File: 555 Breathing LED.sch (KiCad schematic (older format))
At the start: 7 parts, among them Q1 Q_NPN_BCE, U1 LMC555xN

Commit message: update
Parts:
- added BT1: Battery_Cell, Battery:BatteryHolder_Keystone_107_1x23mm, symbol Device:Battery_Cell
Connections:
- net labels added: VCC
- net labels removed: +5V
- wire segments 26 -> 28
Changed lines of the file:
@@
 Wire Wire Line
 	4300 3100 4300 2400
-Wire Wire Line
-	4300 2200 4300 2400
-Connection ~ 4300 2400
 $Comp
 L Timer:LMC555xN U1
@@
 	1    0    0    -1
 $EndComp
-$Comp
-L power:+5V #PWR0103
-U 1 1 613DEE59
-P 4300 2200
-F 0 "#PWR0103" H 4300 2050 50  0001 C CNN
-F 1 "+5V" H 4315 2373 50  0000 C CNN
-F 2 "" H 4300 2200 50  0001 C CNN
-F 3 "" H 4300 2200 50  0001 C CNN
-	1    4300 2200
-	1    0    0    -1
-$EndComp
-$Comp
-L power:+5V #PWR0104
-U 1 1 613E1C2C
-P 6750 2200
-F 0 "#PWR0104" H 6750 2050 50  0001 C CNN
-F 1 "+5V" H 6765 2373 50  0000 C CNN
-F 2 "" H 6750 2200 50  0001 C CNN
-F 3 "" H 6750 2200 50  0001 C CNN
-	1    6750 2200
-	1    0    0    -1
-$EndComp
-Wire Wire Line
-	6750 2200 6750 2500
 $Comp
 L Device:R_US R2
@@
 	6300 2700 6350 2700
 Connection ~ 6350 2700
+$Comp
+L power:GND #PWR0103
+U 1 1 613D1761
+P 3550 3800
+F 0 "#PWR0103" H 3550 3550 50  0001 C CNN
+F 1 "GND" H 3555 3627 50  0000 C CNN
+F 2 "" H 3550 3800 50  0001 C CNN
+F 3 "" H 3550 3800 50  0001 C CNN
+	1    3550 3800
+	1    0    0    -1
+$EndComp
+$Comp
+L power:VCC #PWR0104
+U 1 1 613D37AA
+P 4300 2300
+F 0 "#PWR0104" H 4300 2150 50  0001 C CNN
+F 1 "VCC" H 4315 2473 50  0000 C CNN
+F 2 "" H 4300 2300 50  0001 C CNN
+F 3 "" H 4300 2300 50  0001 C CNN
+	1    4300 2300
+	1    0    0    -1
+$EndComp
+Wire Wire Line
+	4300 2300 4300 2400
+Connection ~ 4300 2400
+$Comp
+L power:VCC #PWR0106
+U 1 1 613D7D24
+P 6750 2250
+F 0 "#PWR0106" H 6750 2100 50  0001 C CNN
+F 1 "VCC" H 6765 2423 50  0000 C CNN
+F 2 "" H 6750 2250 50  0001 C CNN
+F 3 "" H 6750 2250 50  0001 C CNN
+	1    6750 2250
+	1    0    0    -1
+$EndComp
+Wire Wire Line
+	6750 2250 6750 2500
+$Comp
+L power:VCC #PWR0107
+U 1 1 613D98F6
+P 3550 2300
+F 0 "#PWR0107" H 3550 2150 50  0001 C CNN
+F 1 "VCC" H 3565 2473 50  0000 C CNN
+F 2 "" H 3550 2300 50  0001 C CNN
+F 3 "" H 3550 2300 50  0001 C CNN
+	1    3550 2300
+	1    0    0    -1
+$EndComp
+$Comp
+L Device:Battery_Cell BT1
+U 1 1 613DA15B
+P 3550 3100
+F 0 "BT1" H 3668 3196 50  0000 L CNN
+F 1 "Battery_Cell" H 3668 3105 50  0000 L CNN
+F 2 "Battery:BatteryHolder_Keystone_107_1x23mm" V 3550 3160 50  0001 C CNN
+F 3 "~" V 3550 3160 50  0001 C CNN
+	1    3550 3100
+	1    0    0    -1
+$EndComp
+Wire Wire Line
+	3550 2300 3550 2900
+Wire Wire Line
+	3550 3200 3550 3800
 $EndSCHEMATC

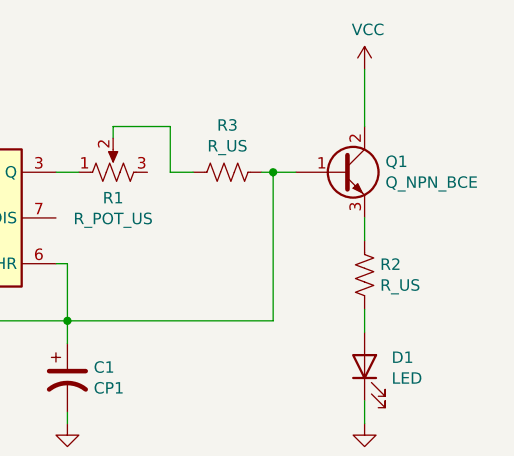
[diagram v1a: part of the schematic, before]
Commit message: Fixed BJT
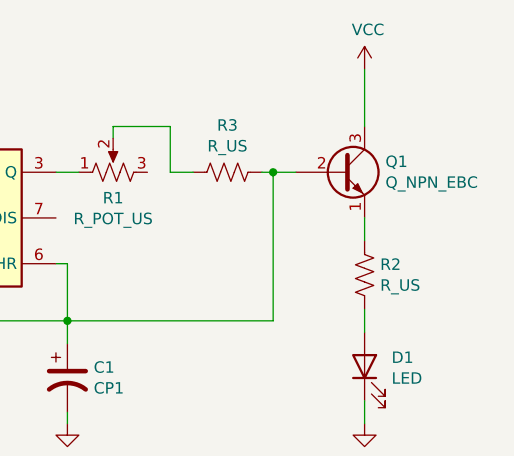
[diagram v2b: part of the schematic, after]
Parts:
- removed Q1: Q_NPN_BCE, Package_TO_SOT_THT:TO-92L_Wide, symbol Device:Q_NPN_BCE
- added Q1: Q_NPN_EBC, Package_TO_SOT_THT:TO-92L_Wide, symbol Device:Q_NPN_EBC
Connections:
- net VCC: now also Q1.3 (C)
- net at C1.1, R3.1, U1.2 (TR)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: now also Q1.2 (B)
- net at R2.1: now also Q1.1 (E)
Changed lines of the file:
@@
 	4900 3300 4900 3800
-$Comp
-L Device:Q_NPN_BCE Q1
-U 1 1 613DCEB1
-P 6650 2700
-F 0 "Q1" H 6841 2746 50  0000 L CNN
-F 1 "Q_NPN_BCE" H 6841 2655 50  0000 L CNN
-F 2 "Package_TO_SOT_THT:TO-92L_Wide" H 6850 2800 50  0001 C CNN
-F 3 "~" H 6650 2700 50  0001 C CNN
-	1    6650 2700
-	1    0    0    -1
-$EndComp
 $Comp
 L Device:R_US R2
@@
 Wire Wire Line
 	3550 3200 3550 3800
+$Comp
+L Device:Q_NPN_EBC Q1
+U 1 1 613D5D1E
+P 6650 2700
+F 0 "Q1" H 6841 2746 50  0000 L CNN
+F 1 "Q_NPN_EBC" H 6841 2655 50  0000 L CNN
+F 2 "Package_TO_SOT_THT:TO-92L_Wide" H 6850 2800 50  0001 C CNN
+F 3 "https://my.centralsemi.com/datasheets/PN2221-2222A.PDF" H 6650 2700 50  0001 C CNN
+	1    6650 2700
+	1    0    0    -1
+$EndComp
 $EndSCHEMATC
